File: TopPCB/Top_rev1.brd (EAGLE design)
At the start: 100 x 80 mm, 5 parts, among them IC1 74HC595D

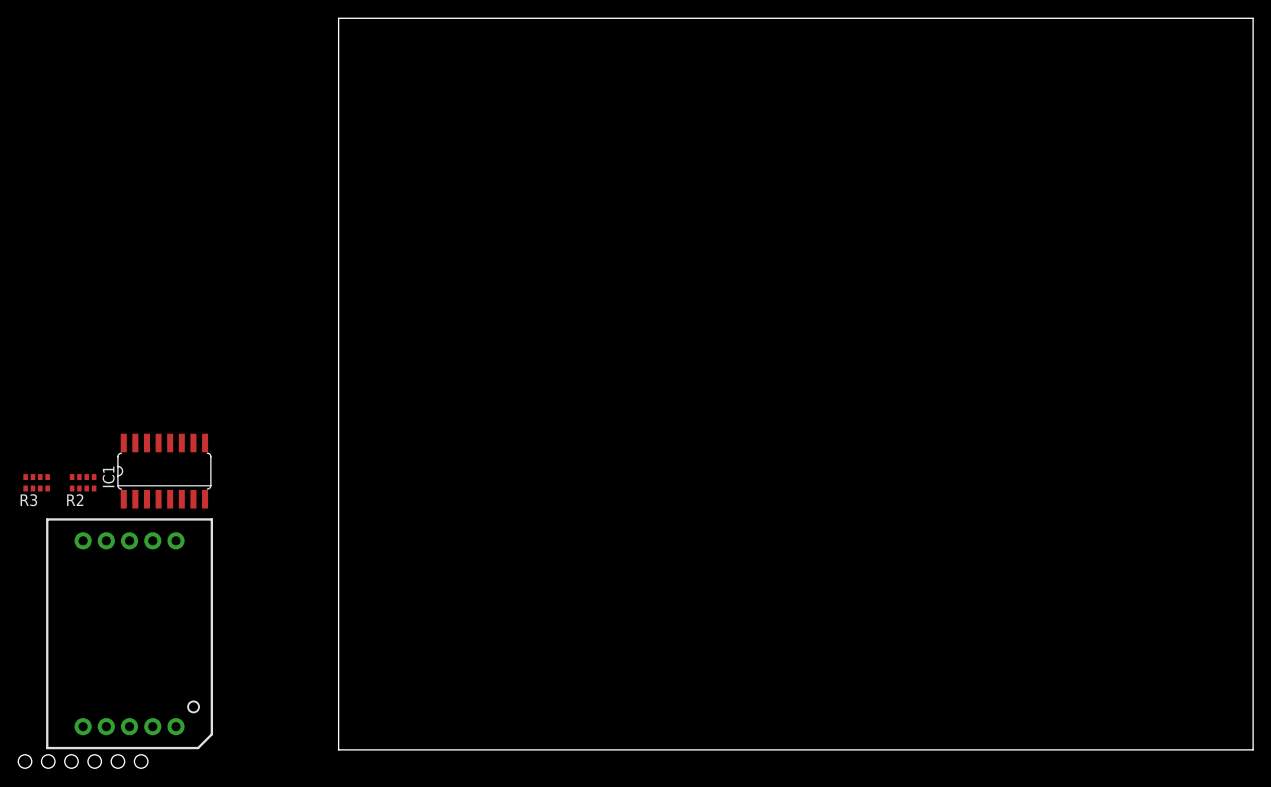
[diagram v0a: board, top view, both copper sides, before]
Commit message: layout board and route traces. changed a few signals between shift register and 7 segment
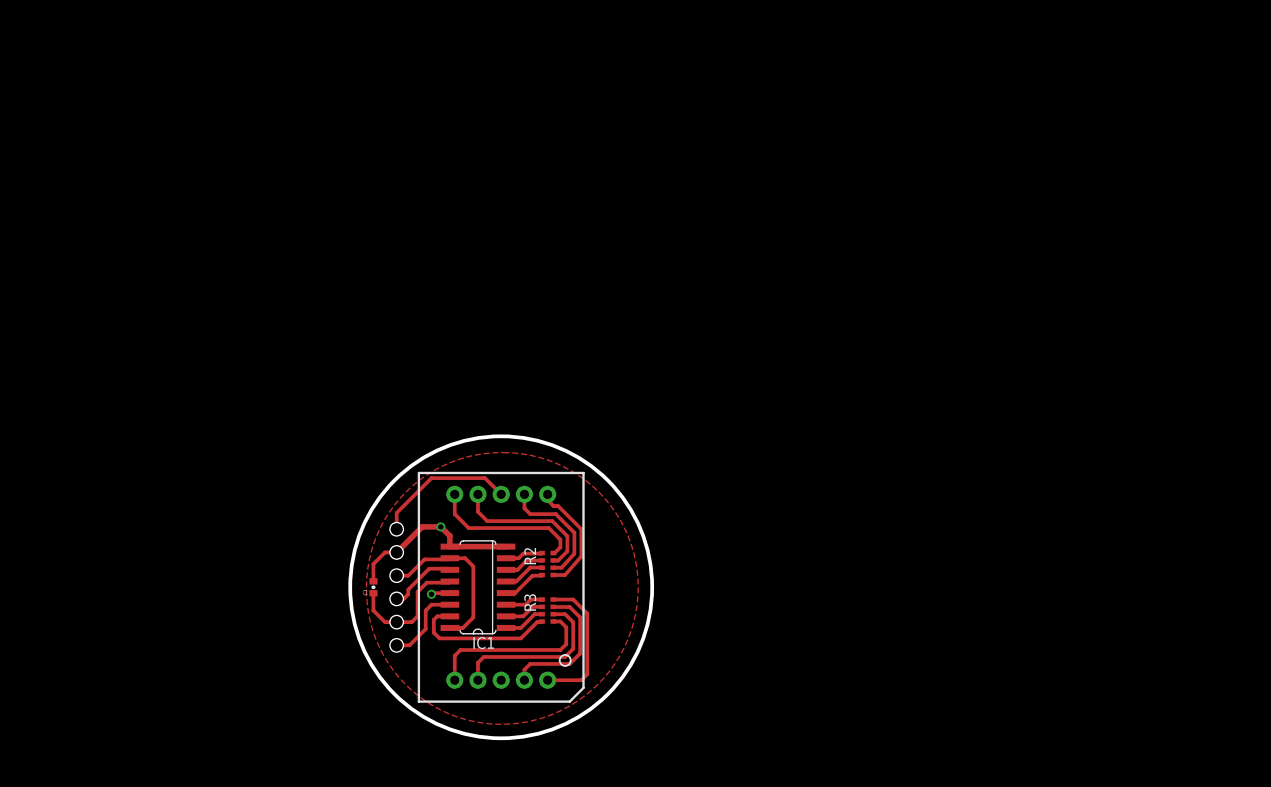
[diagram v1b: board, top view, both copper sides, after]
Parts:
- added C1: 0.1uF, SparkFun-Capacitors:0402-CAP
- JP1: value (none) -> 6 PIN 90degree Header
- R2, R3: value (none) -> 220
- moved R3 57.6 mm to (22.9, 15.2), turned to 270 degrees
- moved R2 51.6 mm to (22.9, 20.3), turned to 270 degrees
- moved JP1 47.9 mm to (6.35, 24.1), turned to 270 degrees
- moved U$1 41.0 mm to (17.8, 17.8)
- moved IC1 36.6 mm to (15.2, 17.8), turned to 90 degrees
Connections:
- removed net N$6: R3.7, U$1.2
- new net N$19: R3.6, U$1.2
- net GND: now also C1.2, JP1.2; no longer JP1.1, U$1.8
- net INPUT+: now also JP1.1, U$1.8; no longer JP1.3, U$1.3
- net N$1: now also R3.8; no longer R3.5
- net N$3: now also R3.5; no longer R3.6
- net N$7: now also R3.7; no longer R3.8
- net RCK: now also C1.1
- net VCC: now also JP1.3; no longer JP1.2
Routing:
- net GND: track 0.00 -> 21.7 mm, vias 0 -> 1
- net N$3: track 0.00 -> 18.9 mm
- net N$19: track 0.00 -> 18.4 mm
- net VCC: track 0.00 -> 18.2 mm
- net N$16: track 0.00 -> 16.7 mm
- net N$15: track 0.00 -> 16.4 mm
- net N$9: track 0.00 -> 16.2 mm
- net N$1: track 0.00 -> 15.6 mm
- net INPUT+: track 0.00 -> 15.5 mm
- net N$7: track 0.00 -> 15.3 mm
- net RCK: track 0.00 -> 14.2 mm
- net N$14: track 0.00 -> 13.4 mm
- net N$8: track 0.00 -> 12.6 mm
- net SERIAL: track 0.00 -> 8.85 mm
- net SCK: track 0.00 -> 7.53 mm
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- added copper zone on layer 1, net GND
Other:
- board size 100 x 80 mm -> 33 x 33 mm

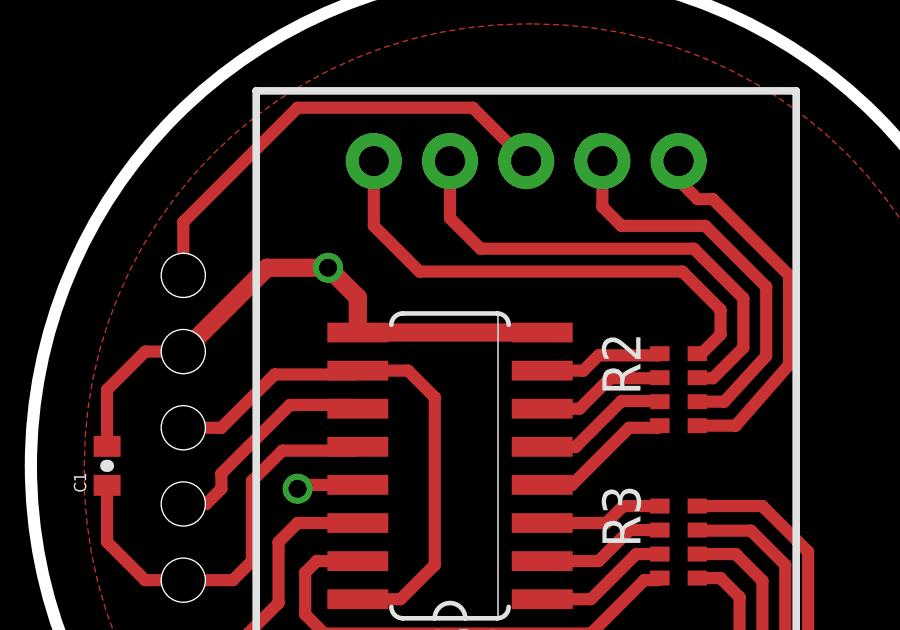
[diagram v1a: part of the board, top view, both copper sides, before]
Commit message: remove ground connection on pin 9 of shift register
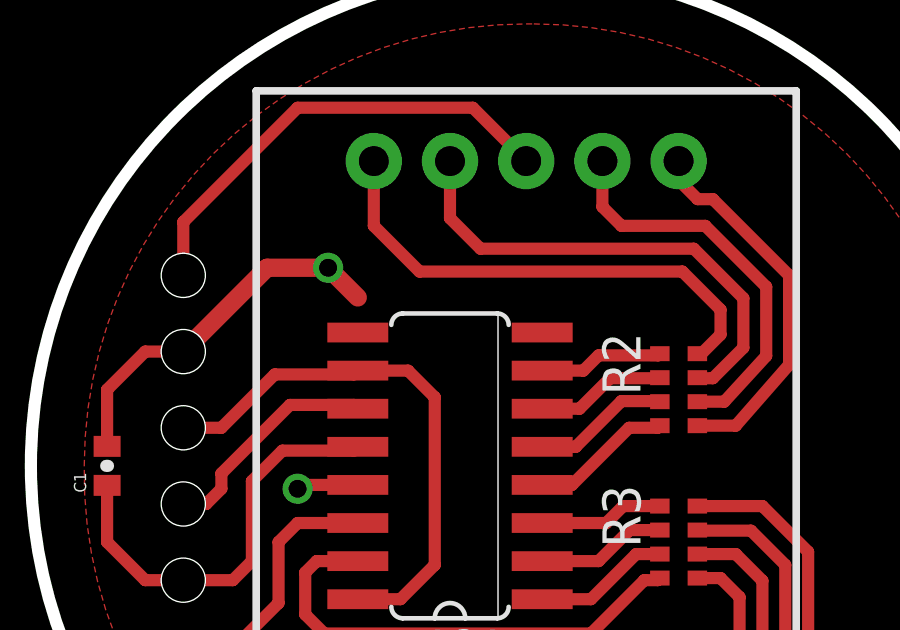
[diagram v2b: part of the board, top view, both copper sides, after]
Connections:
- new net NC: IC1.9, U$1.3
- net GND: no longer IC1.9
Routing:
- net GND: track 21.7 -> 14.4 mm
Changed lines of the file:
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@@
 <signal name="GND">
 <contactref element="IC1" pad="8"/>
-<contactref element="IC1" pad="9"/>
 <contactref element="IC1" pad="13"/>
 <contactref element="C1" pad="2"/>
@@
 <wire x1="10.287" y1="17.145" x2="10.16" y2="17.018" width="0.4064" layer="1"/>
 <via x="11.176" y="24.384" extent="1-16" drill="0.6"/>
-<wire x1="18.3134" y1="22.225" x2="12.1666" y2="22.225" width="0.6096" layer="1"/>
-<wire x1="12.1666" y1="22.225" x2="12.1666" y2="23.3934" width="0.6096" layer="1"/>
 <wire x1="12.1666" y1="23.3934" x2="11.176" y2="24.384" width="0.6096" layer="1"/>
 <wire x1="11.176" y1="24.384" x2="9.144" y2="24.384" width="0.6096" layer="1"/>
@@
 <vertex x="17.78" y="2.794" curve="-90.979389"/>
 </polygon>
-<wire x1="12.1666" y1="22.225" x2="12.1666" y2="17.145" width="0" layer="19" extent="1-1"/>
+<wire x1="10.287" y1="17.145" x2="6.35" y2="21.59" width="0" layer="19" extent="1-1"/>
 </signal>
 <signal name="VCC">
@@
 <via x="10.16" y="17.018" extent="1-16" drill="0.6"/>
 </signal>
+<signal name="NC">
+<contactref element="U$1" pad="3"/>
+<contactref element="IC1" pad="9"/>
+<wire x1="17.78" y1="7.62" x2="12.1666" y2="22.225" width="0" layer="19" extent="1-1"/>
+</signal>
 </signals>

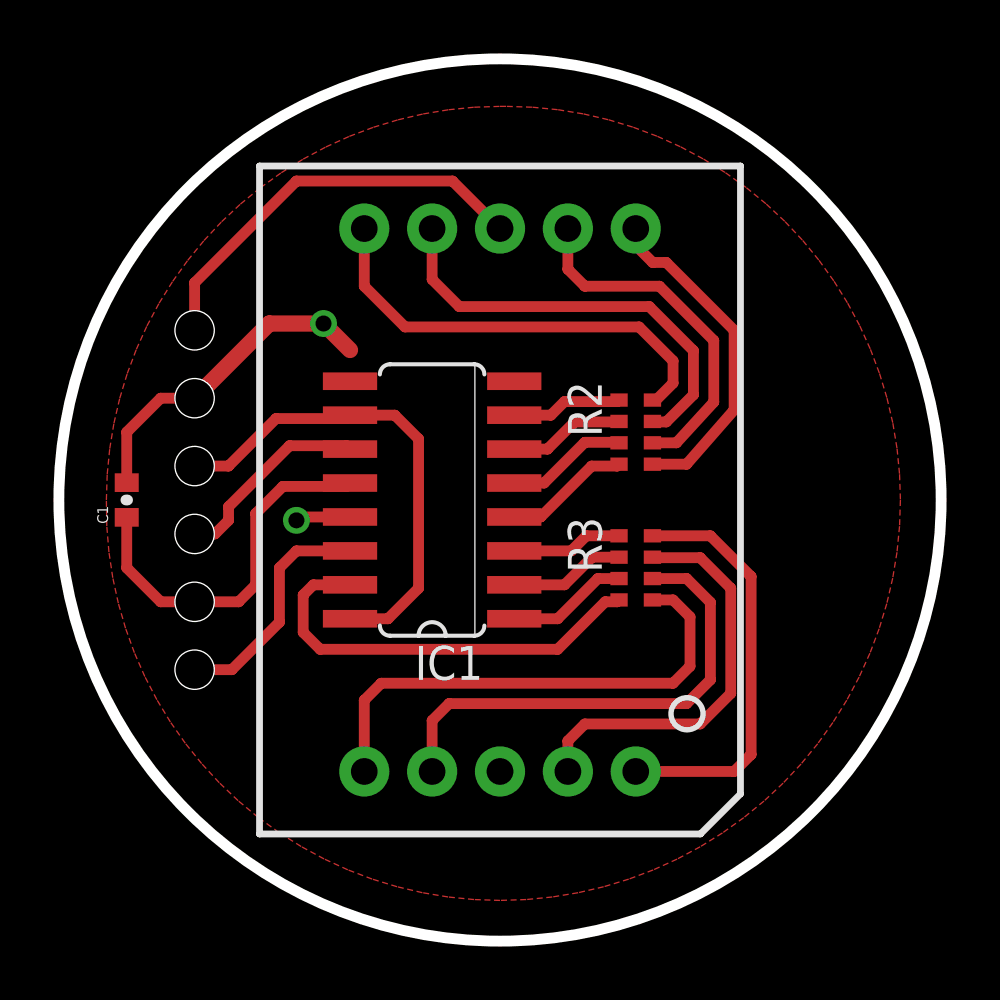
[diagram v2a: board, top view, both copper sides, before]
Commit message: remove BottomPCB folder, finished version 1 of TopPCB, moved Bottom_rev1 to TopPCB folder, first commit of Bottom pcb work.
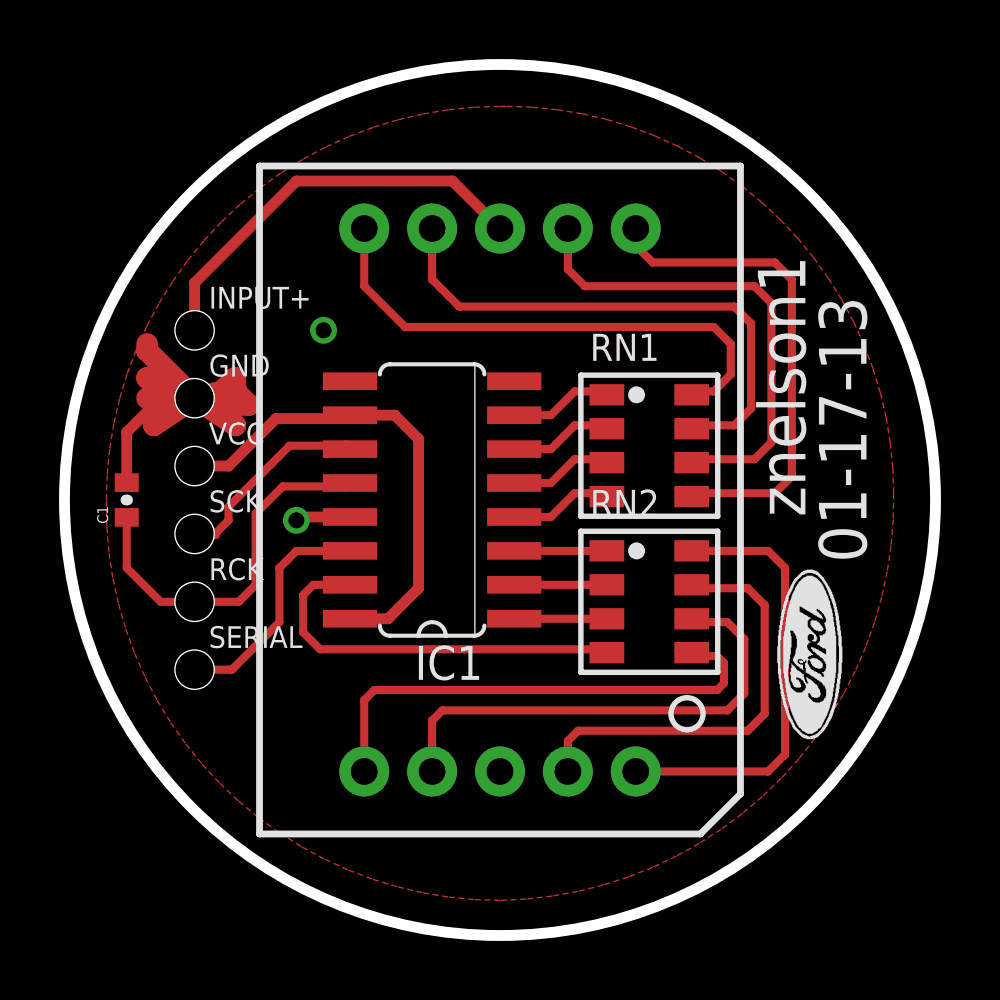
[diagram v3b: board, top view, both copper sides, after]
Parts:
- removed R2, R3: 220, SparkFun-Resistors:0603-ARV
- added RN1, RN2: 220, resistor-array:744-8
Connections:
- removed net NC: IC1.9, U$1.3
- new net NC1: U$1.3
- new net NC2: IC1.9
- net N$1: now also RN2.8; no longer R3.8
- net N$10: now also RN1.4; no longer R2.4
- net N$11: now also RN1.3; no longer R2.3
- net N$12: now also RN1.2; no longer R2.2
- net N$13: now also RN1.1; no longer R2.1
- net N$14: now also RN1.6; no longer R2.6
- net N$15: now also RN1.7; no longer R2.7
- net N$16: now also RN1.8; no longer R2.8
- net N$19: now also RN2.6; no longer R3.6
- net N$2: now also RN2.3; no longer R3.3
- net N$3: now also RN2.5; no longer R3.5
- net N$4: now also RN2.2; no longer R3.2
- net N$5: now also RN2.1; no longer R3.1
- net N$7: now also RN2.7; no longer R3.7
- net N$8: now also RN1.5; no longer R2.5
- net N$9: now also RN2.4; no longer R3.4
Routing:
- net GND: track 14.4 -> 28.4 mm
- net N$8: track 12.6 -> 18.4 mm
- net N$14: track 13.4 -> 18.2 mm
- net N$15: track 16.4 -> 20.2 mm
- net N$16: track 16.7 -> 19.7 mm
- net N$2: track 4.54 -> 3.47 mm
- net N$1: track 15.6 -> 16.6 mm
- net N$9: track 16.2 -> 15.2 mm
- net N$4: track 4.35 -> 3.47 mm
- net N$7: track 15.3 -> 16.1 mm
- net N$10: track 4.74 -> 4.14 mm
- net N$5: track 4.16 -> 3.65 mm
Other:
- board size 33 x 33 mm -> 32.6 x 32.6 mm
- board text added: "01-17-13"
- board text added: "GND"
- board text added: "INPUT+"
- board text added: "RCK"
- board text added: "SCK"
- board text added: "SERIAL"
- board text added: "VCC"
- board text added: "znelson1"
